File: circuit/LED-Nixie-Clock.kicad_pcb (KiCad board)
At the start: 2 copper layers, 213.4 x 43.2 mm, 197 parts, among them J1 USB Micro, J3 Boot, SW1 Reset, U1 MCP1700-3302E_SOT23, U2 STM32F103C8Tx, Y1 8MHz, Y2 32.768kHz

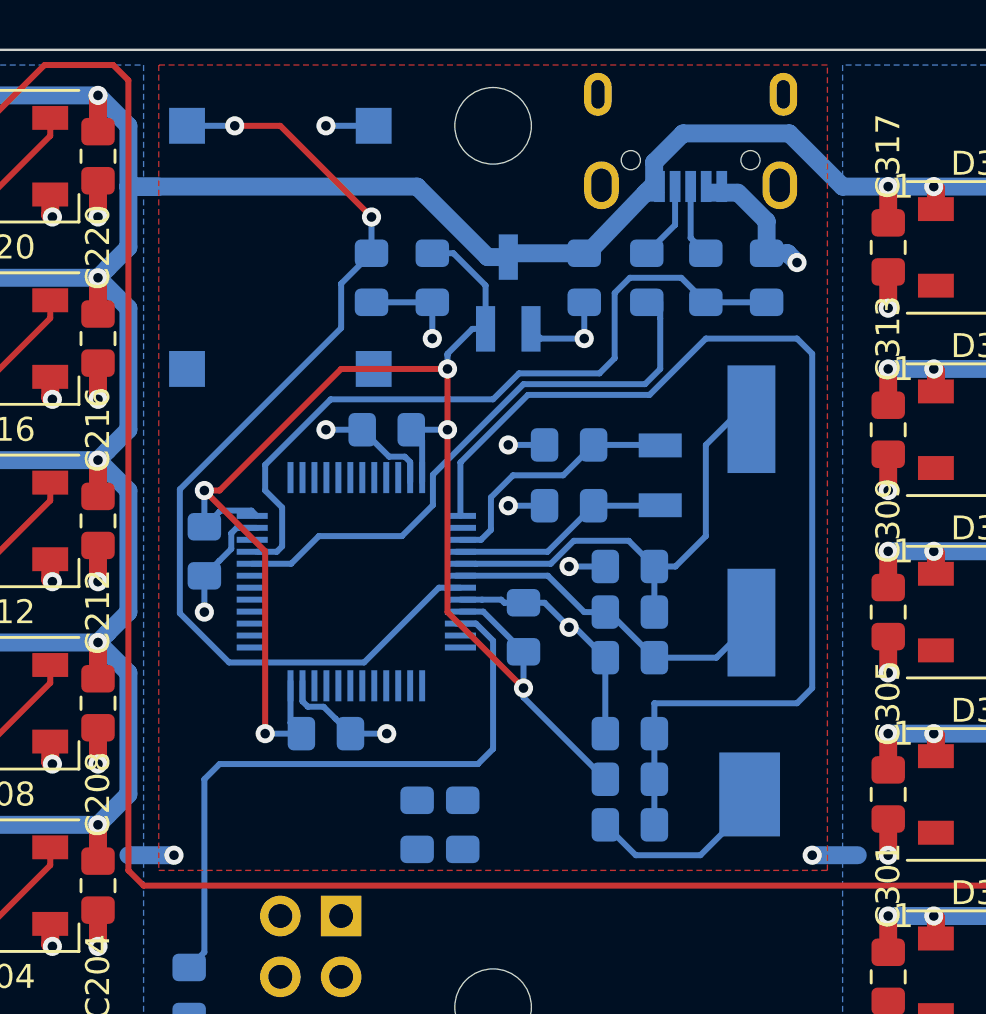
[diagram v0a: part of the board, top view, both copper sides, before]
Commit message: Add SWD/JTAG debug port
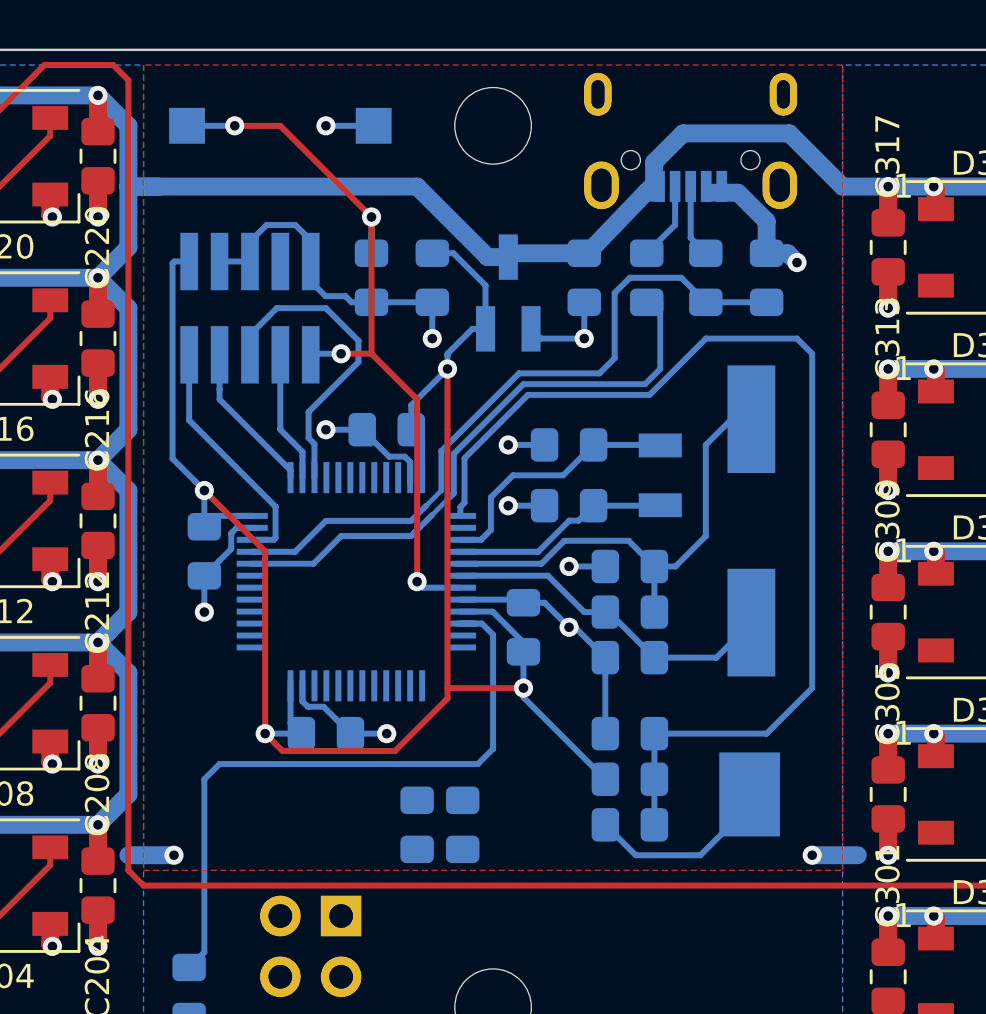
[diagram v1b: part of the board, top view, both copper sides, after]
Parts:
- removed the SW1 at (146.7, 87.6)
- added J2: Debug, Connector_PinHeader_1.27mm:PinHeader_2x05_P1.27mm_Vertical_SMD, B.Cu at (145.4, 85.1)
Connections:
- U2 pad 34: (no net) -> /SWDIO-JTMS
- U2 pad 37: (no net) -> /SWCLK-JTCK
- U2 pad 38: (no net) -> /JTDI
- U2 pad 39: (no net) -> /SWO-JTDO
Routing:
- net /SWO-JTDO: track 0.00 -> 13.1 mm
- net /RESET: track 43.0 -> 31.3 mm, vias 2 -> 4
- net VDD: track 67.3 -> 78.5 mm, vias 5 -> 4
- net /SWDIO-JTMS: track 0.00 -> 10.2 mm
- net GND: track 247.8 -> 257.6 mm
- net /SWCLK-JTCK: track 0.00 -> 6.36 mm
- net /JTDI: track 0.00 -> 5.51 mm
- net /USBDP: track 30.4 -> 28.6 mm
- net Net-(R7-Pad2): track 27.1 -> 27.9 mm
- net +BATT: track 45.2 -> 44.5 mm

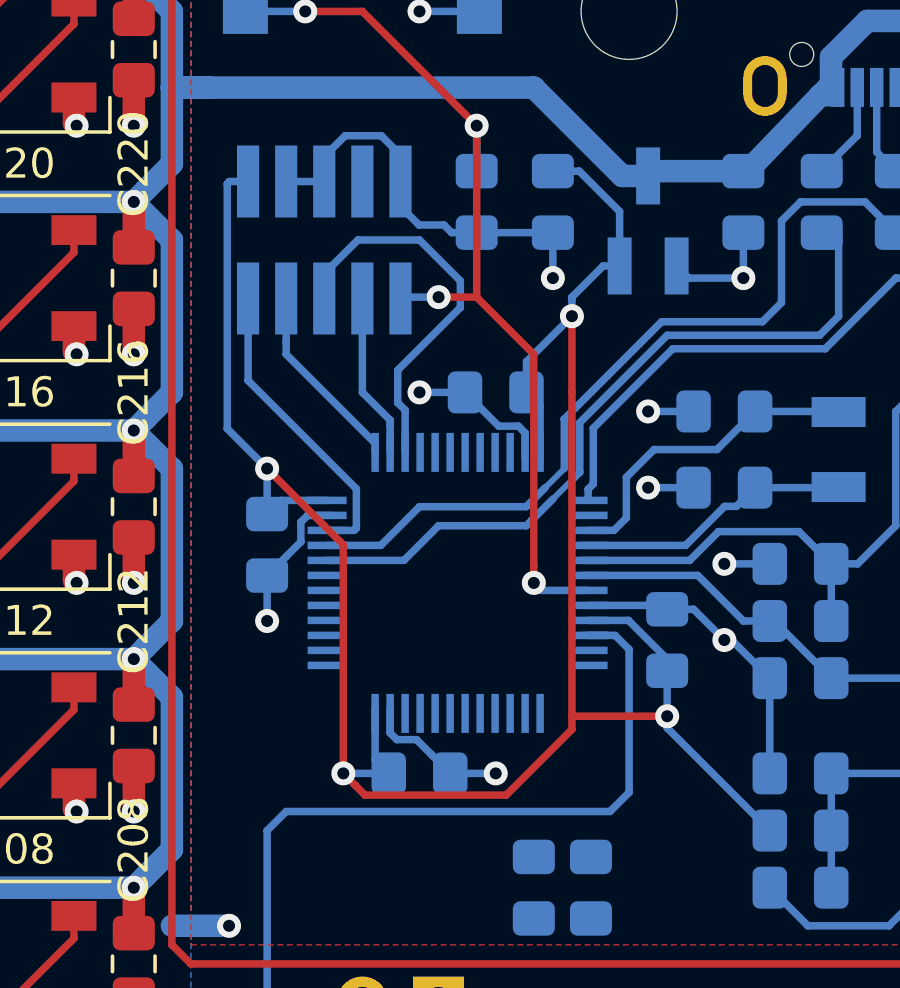
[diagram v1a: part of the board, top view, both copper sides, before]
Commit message: Fix DRC problems
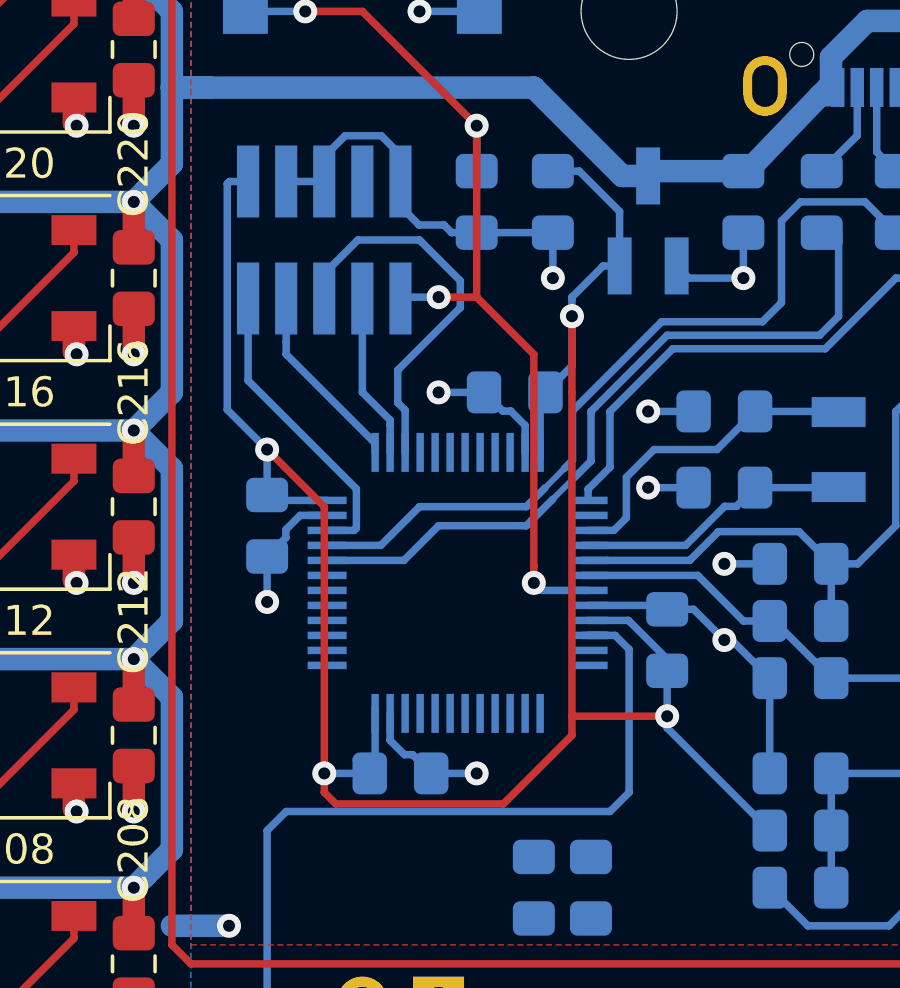
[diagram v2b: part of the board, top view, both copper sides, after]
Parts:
- moved C8 0.64 mm to (143.5, 94.6)
- moved C7 0.63 mm to (148.0, 102.9)
- moved C9 0.63 mm to (151.8, 90.2)
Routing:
- net GND: track 257.6 -> 255.6 mm

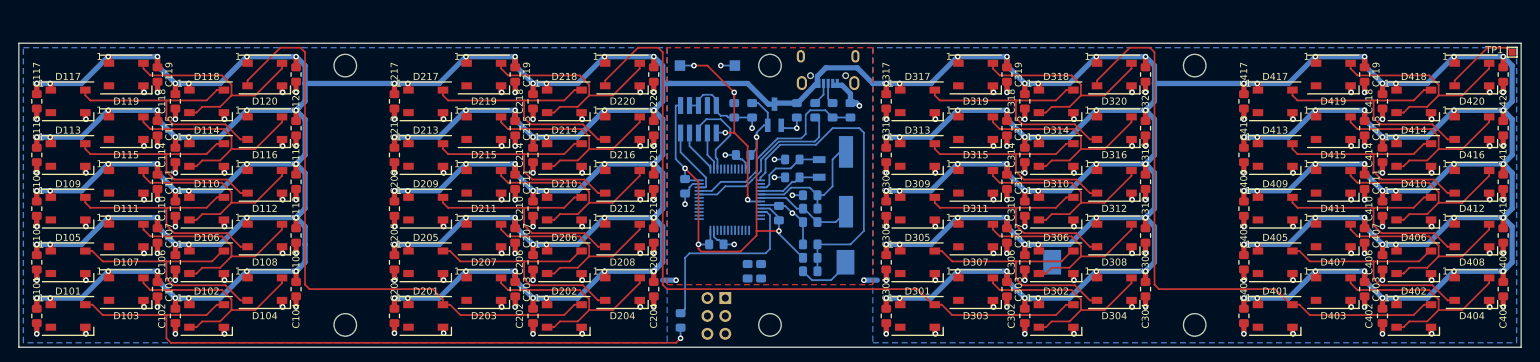
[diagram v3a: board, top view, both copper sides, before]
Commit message: Fix GND zone filling
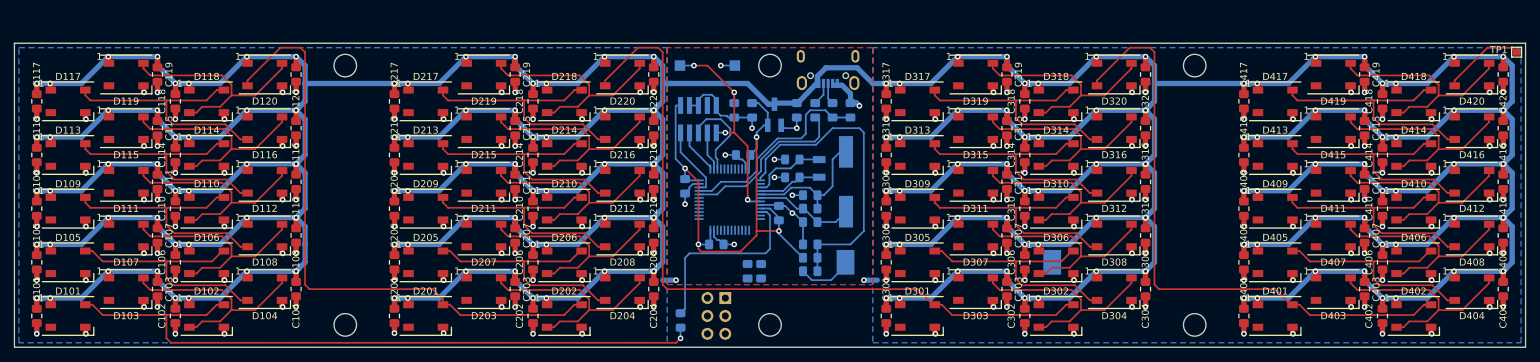
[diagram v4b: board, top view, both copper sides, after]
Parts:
- moved TP1 0.63 mm to (261.6, 75.6)
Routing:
- net /Digit 4/DOUT: track 11.1 -> 11.7 mm
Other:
- board size 213.4 x 43.2 mm -> 214.6 x 43.2 mm
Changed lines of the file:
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@@
   )
   (module TestPoint:TestPoint_Pad_1.0x1.0mm (layer F.Cu)
-    (at 260.985 75.565)
+    (at 261.62 75.565)
     (descr "SMD rectangular pad as test Point, square 1.0mm side length")
     (tags "test point SMD pad rectangle square")
@@
   (gr_line (start 170.18 117.475) (end 170.18 74.295) (layer F.CrtYd) (width 0.1))
   (gr_line (start 140.97 74.295) (end 140.97 117.475) (layer F.CrtYd) (width 0.1))
-  (gr_line (start 262.255 74.295) (end 262.255 117.475) (layer Edge.Cuts) (width 0.1))
+  (gr_line (start 262.89 74.295) (end 262.89 117.475) (layer Edge.Cuts) (width 0.1))
   (gr_line (start 221.4 82.55) (end 261.2 82.55) (layer Dwgs.User) (width 0.2))
   (gr_line (start 221.4 83.95) (end 261.2 83.95) (layer Dwgs.User) (width 0.2))
@@
   (gr_line (start 69.85 111.63) (end 69.85 114.43) (layer Dwgs.User) (width 0.2))
   (gr_line (start 49.95 111.63) (end 89.75 111.63) (layer Dwgs.User) (width 0.2))
-  (gr_line (start 48.895 117.475) (end 48.895 74.295) (layer Edge.Cuts) (width 0.1))
-  (gr_line (start 262.255 117.475) (end 48.895 117.475) (layer Edge.Cuts) (width 0.1))
-  (gr_line (start 48.895 74.295) (end 262.255 74.295) (layer Edge.Cuts) (width 0.1))
+  (gr_line (start 48.26 117.475) (end 48.26 74.295) (layer Edge.Cuts) (width 0.1))
+  (gr_line (start 262.89 117.475) (end 48.26 117.475) (layer Edge.Cuts) (width 0.1))
+  (gr_line (start 48.26 74.295) (end 262.89 74.295) (layer Edge.Cuts) (width 0.1))
   (segment (start 170.815 107.95) (end 168.91 107.95) (width 0.75) (layer B.Cu) (net 1))
   (via (at 142.24 107.95) (size 0.8) (drill 0.4) (layers F.Cu B.Cu) (net 1))
@@
   (via (at 51.435 115.57) (size 0.8) (drill 0.4) (layers F.Cu B.Cu) (net 1))
   (segment (start 51.435 114.055) (end 51.435 115.57) (width 0.75) (layer F.Cu) (net 1))
-  (via (at 88.265 81.28) (size 0.8) (drill 0.4) (layers F.Cu B.Cu) (net 1) (status 1000000))
-  (segment (start 88.265 79.765) (end 88.265 81.28) (width 0.75) (layer F.Cu) (net 1) (status 1000000))
+  (via (at 88.265 81.28) (size 0.8) (drill 0.4) (layers F.Cu B.Cu) (net 1))
+  (segment (start 88.265 79.765) (end 88.265 81.28) (width 0.75) (layer F.Cu) (net 1))
   (via (at 71.12 107.95) (size 0.8) (drill 0.4) (layers F.Cu B.Cu) (net 1))
   (segment (start 71.12 106.435) (end 71.12 107.95) (width 0.75) (layer F.Cu) (net 1))
@@
   (segment (start 238.035 77.14) (end 238.035 77.89) (width 0.25) (layer F.Cu) (net 44))
   (segment (start 239.00999 78.86499) (end 249.214992 78.86499) (width 0.25) (layer F.Cu) (net 44))
-  (segment (start 260.35 74.93) (end 260.985 75.565) (width 0.25) (layer F.Cu) (net 45))
+  (segment (start 260.985 74.93) (end 261.62 75.565) (width 0.25) (layer F.Cu) (net 45))
+  (segment (start 257.48 74.93) (end 260.985 74.93) (width 0.25) (layer F.Cu) (net 45))
   (segment (start 252.82 79.59) (end 257.48 74.93) (width 0.25) (layer F.Cu) (net 45))
-  (segment (start 257.48 74.93) (end 260.35 74.93) (width 0.25) (layer F.Cu) (net 45))
   (segment (start 252.82 80.34) (end 252.82 79.59) (width 0.25) (layer F.Cu) (net 45))
   (segment (start 162.315 95.885) (end 162.315 97.79) (width 0.25) (layer B.Cu) (net 46))
@@
     (polygon
       (pts
-        (xy 49.53 74.93) (xy 140.97 74.93) (xy 140.97 116.84) (xy 49.53 116.84)
+        (xy 48.895 74.93) (xy 140.97 74.93) (xy 140.97 116.84) (xy 48.895 116.84)
       )
     )
@@
     (polygon
       (pts
-        (xy 170.18 74.93) (xy 170.18 116.84) (xy 261.62 116.84) (xy 261.62 74.93)
+        (xy 170.18 74.93) (xy 170.18 116.84) (xy 262.255 116.84) (xy 262.255 74.93)
       )
     )

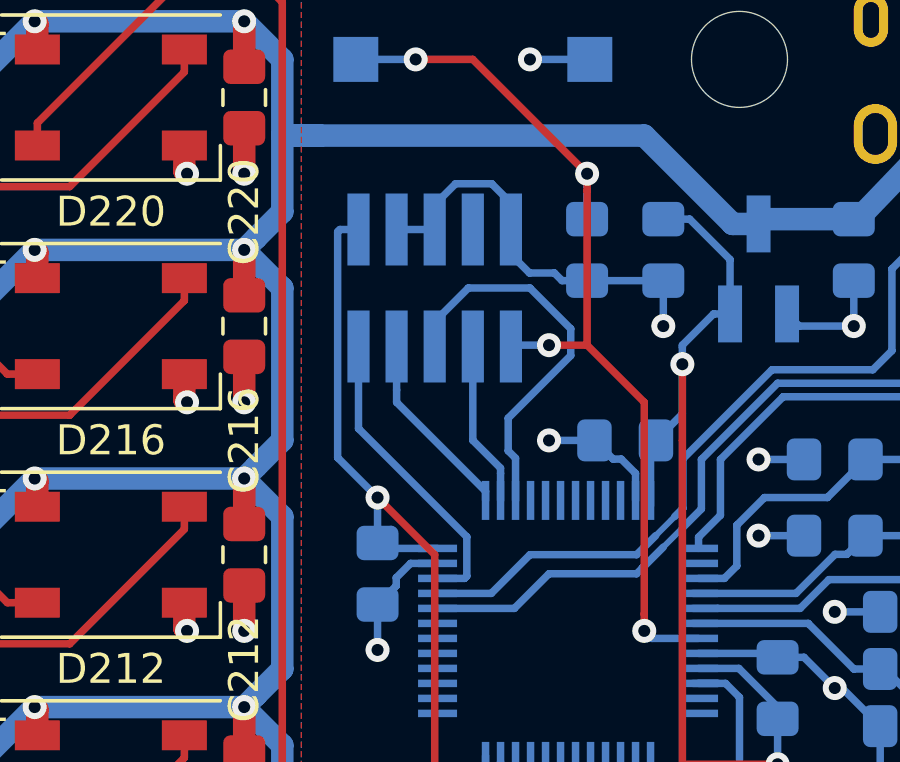
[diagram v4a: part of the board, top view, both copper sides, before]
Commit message: Improve spacing around debug connector
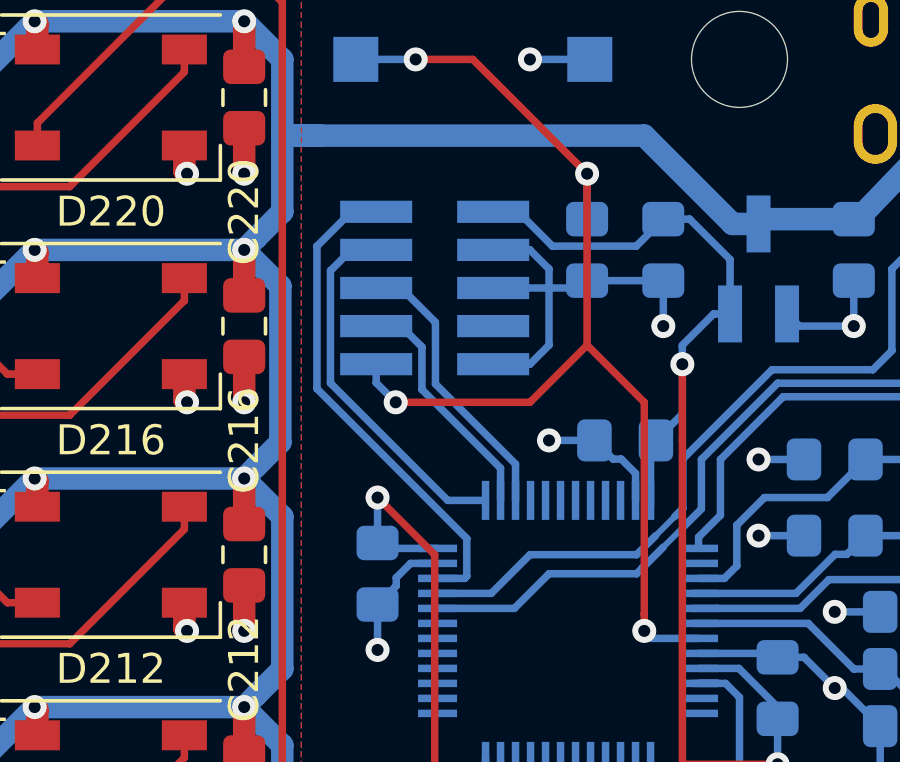
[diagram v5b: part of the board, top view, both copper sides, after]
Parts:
- turned J2 to 180 degrees
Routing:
- net /SWDIO-JTMS: track 10.2 -> 16.5 mm
- net /RESET: track 31.3 -> 37.5 mm
- net /SWCLK-JTCK: track 6.36 -> 12.3 mm
- net VDD: track 78.6 -> 75.0 mm
- net /SWO-JTDO: track 13.1 -> 9.49 mm
- net /JTDI: track 5.51 -> 8.01 mm
